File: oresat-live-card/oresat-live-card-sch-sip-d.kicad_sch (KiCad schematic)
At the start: 7 parts, among them J3 Conn_01x02, U7 OSD3358-512M-BSM

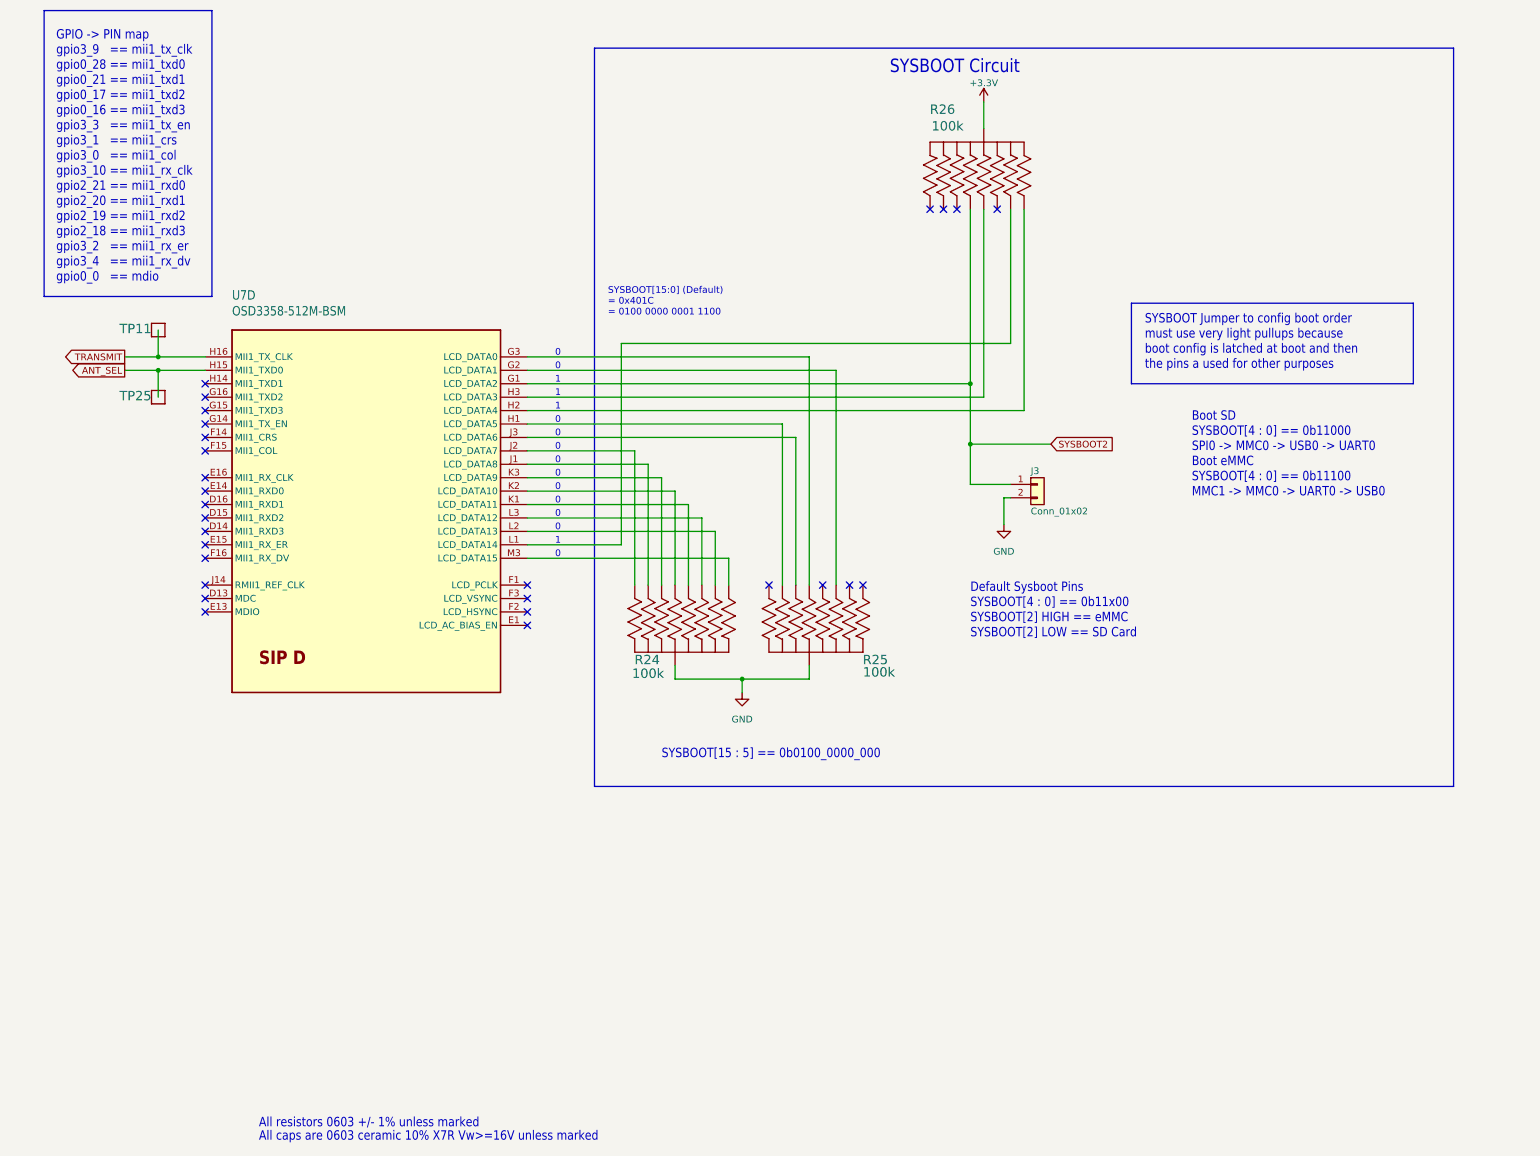
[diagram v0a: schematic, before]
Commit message: Schematic cleaned up and should be good to go. Lots of DRC errors to fix. Also waiting for design review.
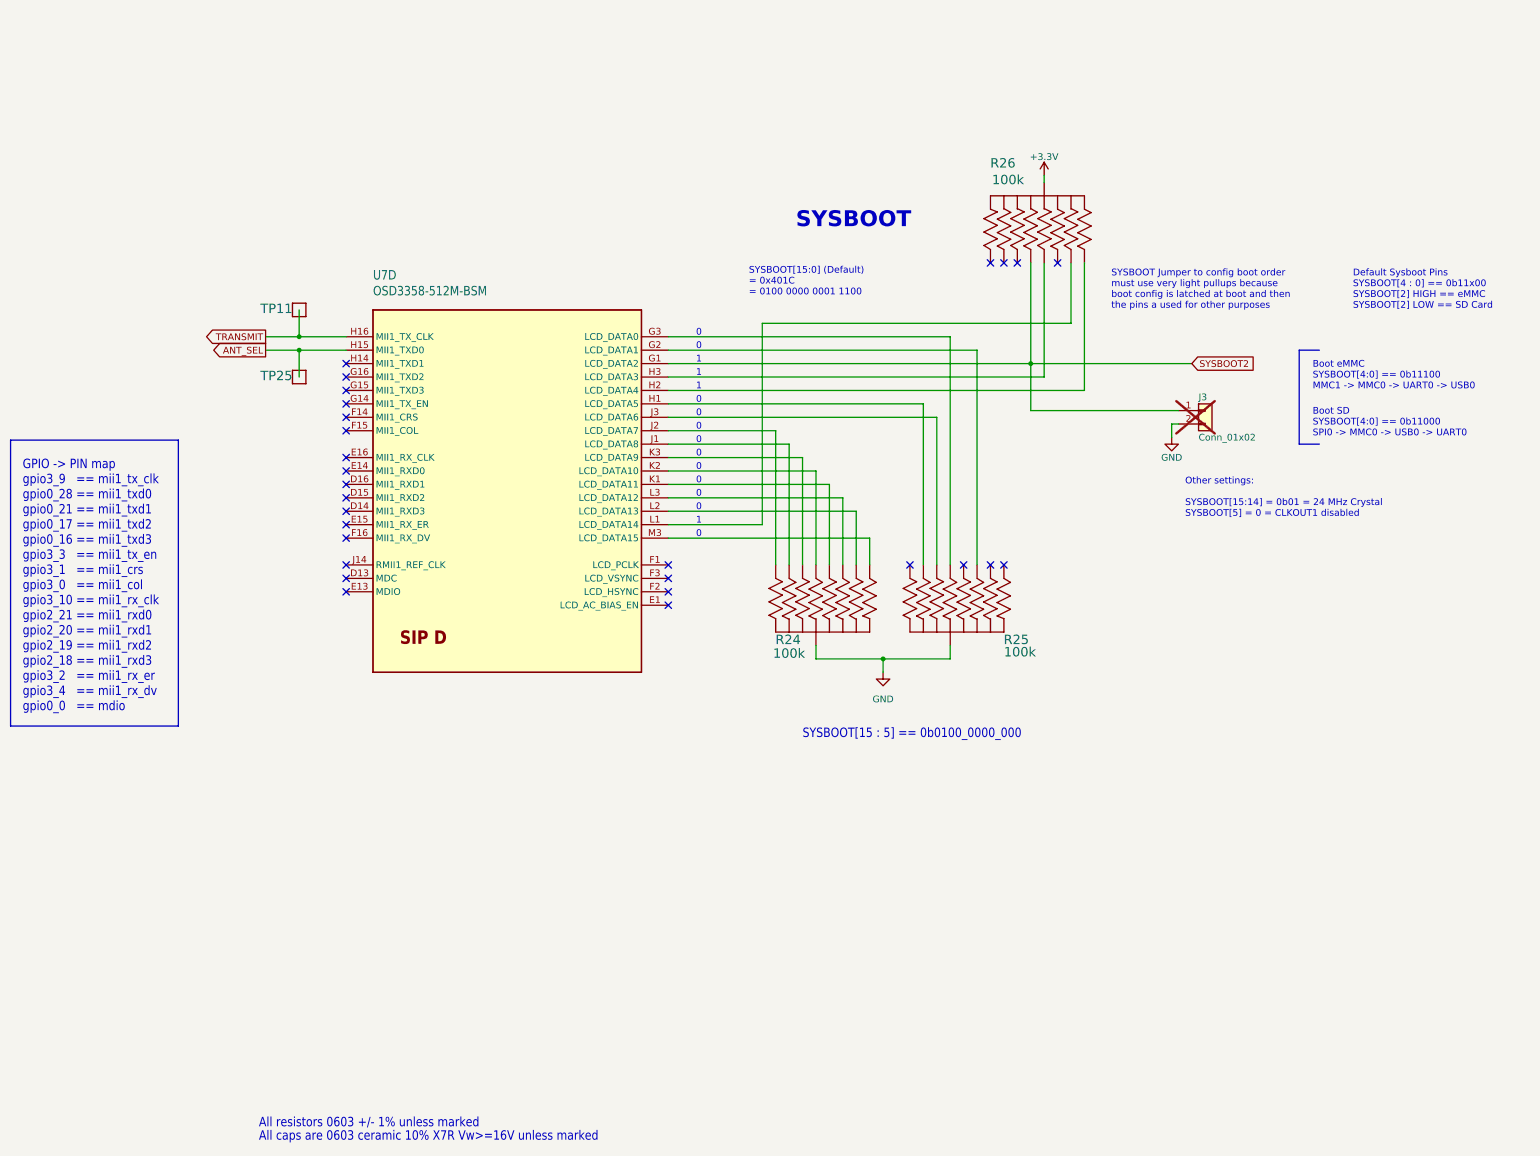
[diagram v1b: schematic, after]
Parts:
- J3: now not fitted
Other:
- note added: "Boot SD SYSBOOT[4:0] == 0b11000 SPI0 -> MMC0 -> USB0 -> UART0"
- note added: "Boot eMMC SYSBOOT[4:0] == 0b11100 MMC1 -> MMC0 -> UART0 -> USB0"
- note added: "Other settings: SYSBOOT[15:14] = 0b01 = 24 MHz Crystal SYSBOOT[5] = 0 = CLKOUT1 disabled"
- note added: "SYSBOOT"
- note removed: "Boot SD SYSBOOT[4 : 0] == 0b11000 SPI0 -> MMC0 -> USB0 -> UART0 Boot eMMC SYSBOOT[4 : 0] == 0b11100 MMC1 -> MMC0 -> UART0 -> USB0"
- note removed: "SYSBOOT Circuit"
- moved on the sheet: R24, R25, R26, TP11, TP25, U7D
